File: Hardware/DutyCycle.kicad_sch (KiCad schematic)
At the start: 42 parts, among them J1 LiPo, J2 USB, Q1 AO3400A, Q2 AO3400A, Q3 AO3401A, SW1 SW_Push, U1 AT32F421KxU7, U2 DRV8837, U3 ME6211C28M5, U5 TP4055

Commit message: feat(sch): rename +2.8v -> VDD
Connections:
- net +2.8V renamed VDD
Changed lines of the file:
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@@
 			)
 		)
-		(property "Value" "+2.8V"
-			(at 193.04 143.51 0)
+		(property "Value" "VDD"
+			(at 195.58 147.3199 0)
 			(effects
 				(font
 					(size 1.27 1.27)
 				)
+				(justify right)
 			)
 		)
@@
 			)
 		)
-		(property "Value" "+2.8V"
-			(at 73.66 140.97 0)
+		(property "Value" "VDD"
+			(at 76.2 144.7799 0)
 			(effects
 				(font
 					(size 1.27 1.27)
 				)
+				(justify left)
 			)
 		)
@@
 			)
 		)
-		(property "Value" "+2.8V"
-			(at 128.27 118.11 0)
+		(property "Value" "VDD"
+			(at 130.81 121.9199 0)
 			(effects
 				(font
 					(size 1.27 1.27)
 				)
+				(justify left)
 			)
 		)
@@
 			)
 		)
-		(property "Value" "+2.8V"
-			(at 195.58 223.52 0)
+		(property "Value" "VDD"
+			(at 198.12 227.3299 0)
 			(effects
 				(font
 					(size 1.27 1.27)
 				)
+				(justify right)
 			)
 		)
@@
 		(on_board yes)
 		(dnp no)
-		(fields_autoplaced yes)
 		(property "Reference" "#PWR026"
 			(at 342.9 57.15 0)
@@
 			)
 		)
-		(property "Value" "+2.8V"
-			(at 342.9 48.26 0)
+		(property "Value" "VDD"
+			(at 344.424 49.276 0)
 			(effects
 				(font
 					(size 1.27 1.27)
 				)
+				(justify left)
 			)
 		)
@@
 			)
 		)
-		(property "Value" "+2.8V"
-			(at 128.27 203.2 0)
+		(property "Value" "VDD"
+			(at 130.81 207.0099 0)
 			(effects
 				(font
 					(size 1.27 1.27)
 				)
+				(justify left)
 			)
 		)

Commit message: feat(Hardware): upload pcb
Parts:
- removed BZ1: Buzzer, symbol Device:Buzzer
- removed C12: 10uF, Capacitor_SMD:C_0402_1005Metric, symbol Device:C
- removed C14: 100nF, Capacitor_SMD:C_0402_1005Metric, symbol Device:C
- removed R10: 0R, Resistor_SMD:R_0402_1005Metric, symbol Device:R
- removed R8: R_Variable, symbol Device:R_Variable
- removed TP5: MOT_OUT1, TestPoint:TestPoint_Pad_D1.0mm, symbol Connector:TestPoint
- removed TP6: MOT_OUT2, TestPoint:TestPoint_Pad_D1.0mm, symbol Connector:TestPoint
- removed U2: DRV8837, Package_SON:WSON-8-1EP_2x2mm_P0.5mm_EP0.9x1.6mm, symbol Driver_Motor:DRV8837
- added J4: MOT, Connector_PinHeader_2.54mm:PinHeader_1x02_P2.54mm_Vertical, symbol Connector:Conn_01x02_Pin
- added LS1: CMT-8530S-SMT, DutyCycle:CUI_CMT-8530S-SMT, symbol DutyCycle:CMT-8530S-SMT
- added R10: 3296P-1-105, DutyCycle:TRIM_3296P-1-105, symbol DutyCycle:3296P-1-105
- J2: footprint Connector_USB:USB_C_Receptacle_G-Switch_GT-USB-7051x -> Connector_USB:USB_C_Receptacle_G-Switch_GT-USB-7010ASV
- SW1: footprint Button_Switch_SMD:SW_Push_1P1T-MP_NO_Horizontal_Alps_SKRTLAE010 -> Button_Switch_THT:SW_Tactile_SPST_Angled_PTS645Vx83-2LFS
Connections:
- net VBAT: now also LS1.P
- net at Q1.3 (D): now also LS1.N
- net MOT_OUT1: now reaches U1.14 (PB0)
- net MOT_OUT1: now also R10.1
- net MOT_OUT2: now reaches U1.15 (PB1)
- net MOT_OUT2: now also J4.2 (Pin_2)
- net DRV_IN1: no longer names the net of U1.9 (PA3)
- net DRV_IN2: no longer names the net of U1.8 (PA2)
- net DRV_SLP: no longer names the net of U1.10 (PA4)
- new net: J4.1 (Pin_1), R10.2
- no-connect marks 16 -> 18

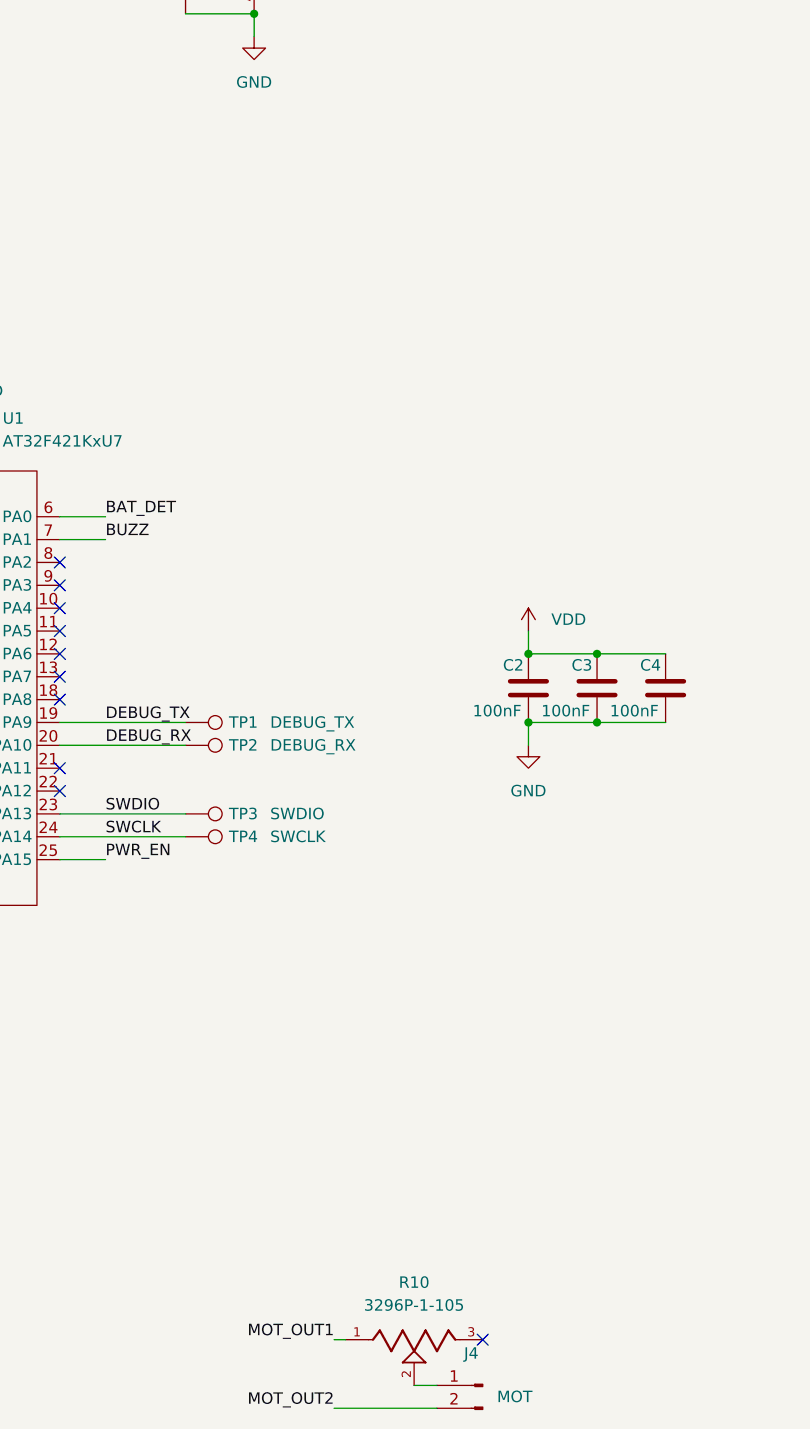
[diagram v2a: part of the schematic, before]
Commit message: feat(pcb): complete the basic layout of components
Signed-off-by: _VIFEXTech <vifextech@foxmail.com>
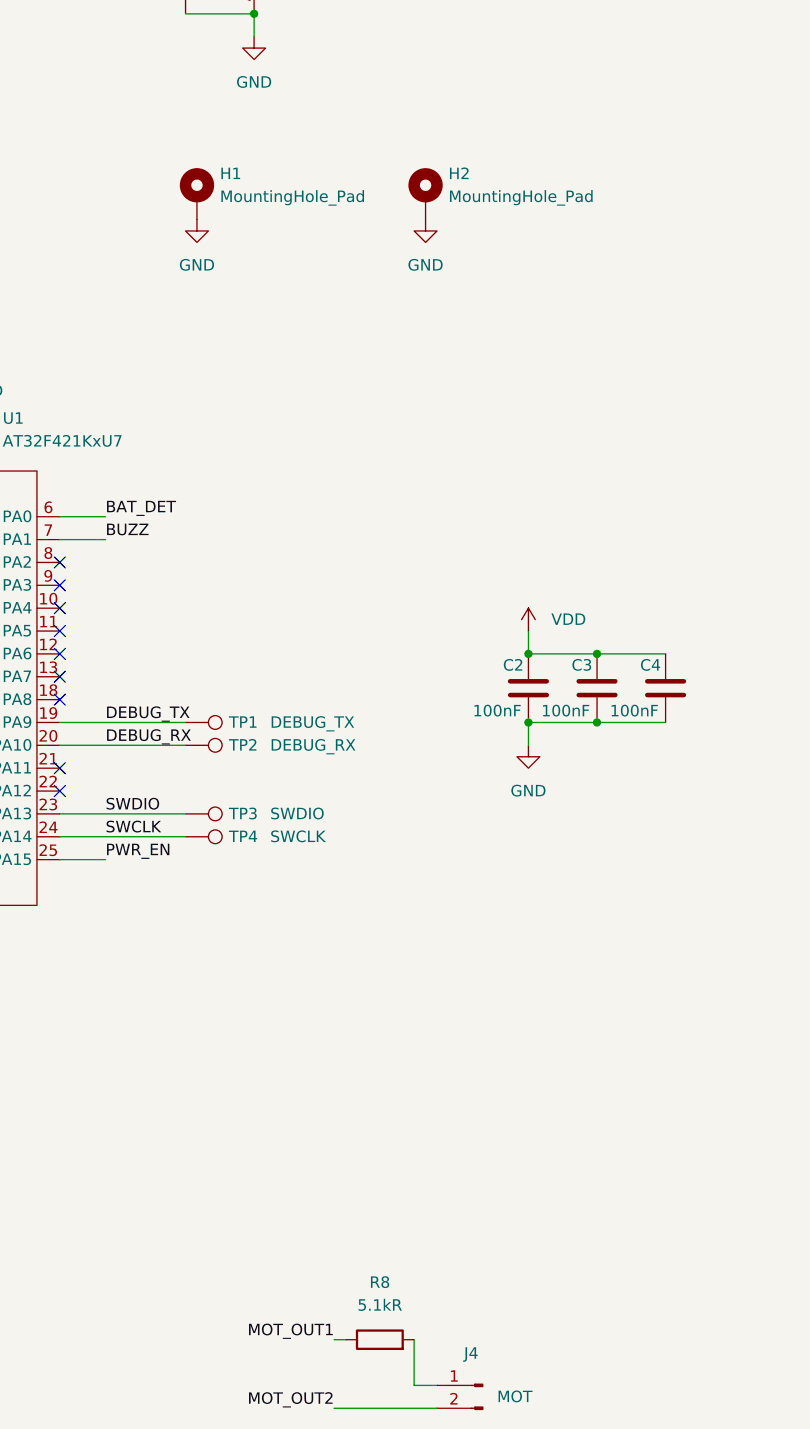
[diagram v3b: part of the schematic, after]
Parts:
- removed R10: 3296P-1-105, DutyCycle:TRIM_3296P-1-105, symbol DutyCycle:3296P-1-105
- added H1, H2: MountingHole_Pad, MountingHole:MountingHole_3.2mm_M3_Pad, symbol Mechanical:MountingHole_Pad
- added R8: 5.1kR, Resistor_SMD:R_0402_1005Metric, symbol Device:R
- J2: footprint Connector_USB:USB_C_Receptacle_G-Switch_GT-USB-7010ASV -> Connector_USB:USB_C_Receptacle_G-Switch_GT-USB-7051x
- SW1: footprint Button_Switch_THT:SW_Tactile_SPST_Angled_PTS645Vx83-2LFS -> Button_Switch_THT:SW_PUSH_6mm_H13mm
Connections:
- net GND: now also H1.1, H2.1
- net MOT_OUT1: now also R8.1
- net at J4.1 (Pin_1): now also R8.2
- no-connect marks 18 -> 17

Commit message: feat(pcb): finish PCB layout
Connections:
- net BAT_DET: now also U1.15 (PB1); no longer U1.6 (PA0)
- net BUZZ: now also U1.16 (PB2); no longer U1.7 (PA1)
- net DEBUG_RX: now also J2.A7 (D-); no longer J2.A6 (D+), J2.B6 (D+)
- net DEBUG_TX: now also J2.A8 (SBU1); no longer J2.A5 (CC1), J2.B5 (CC2)
- net KEY_DET: now also U1.14 (PB0); no longer U1.26 (PB3)
- net MOT_OUT1: now also U1.8 (PA2); no longer U1.14 (PB0)
- net MOT_OUT2: now also U1.9 (PA3); no longer U1.15 (PB1)
- net PWR_EN: now also U1.13 (PA7); no longer U1.25 (PA15)
- net SWCLK: now also J2.A5 (CC1); no longer J2.A8 (SBU1), J2.B8 (SBU2)
- net SWDIO: now also J2.A6 (D+); no longer J2.A7 (D-), J2.B7 (D-)
- no-connect marks 17 -> 21

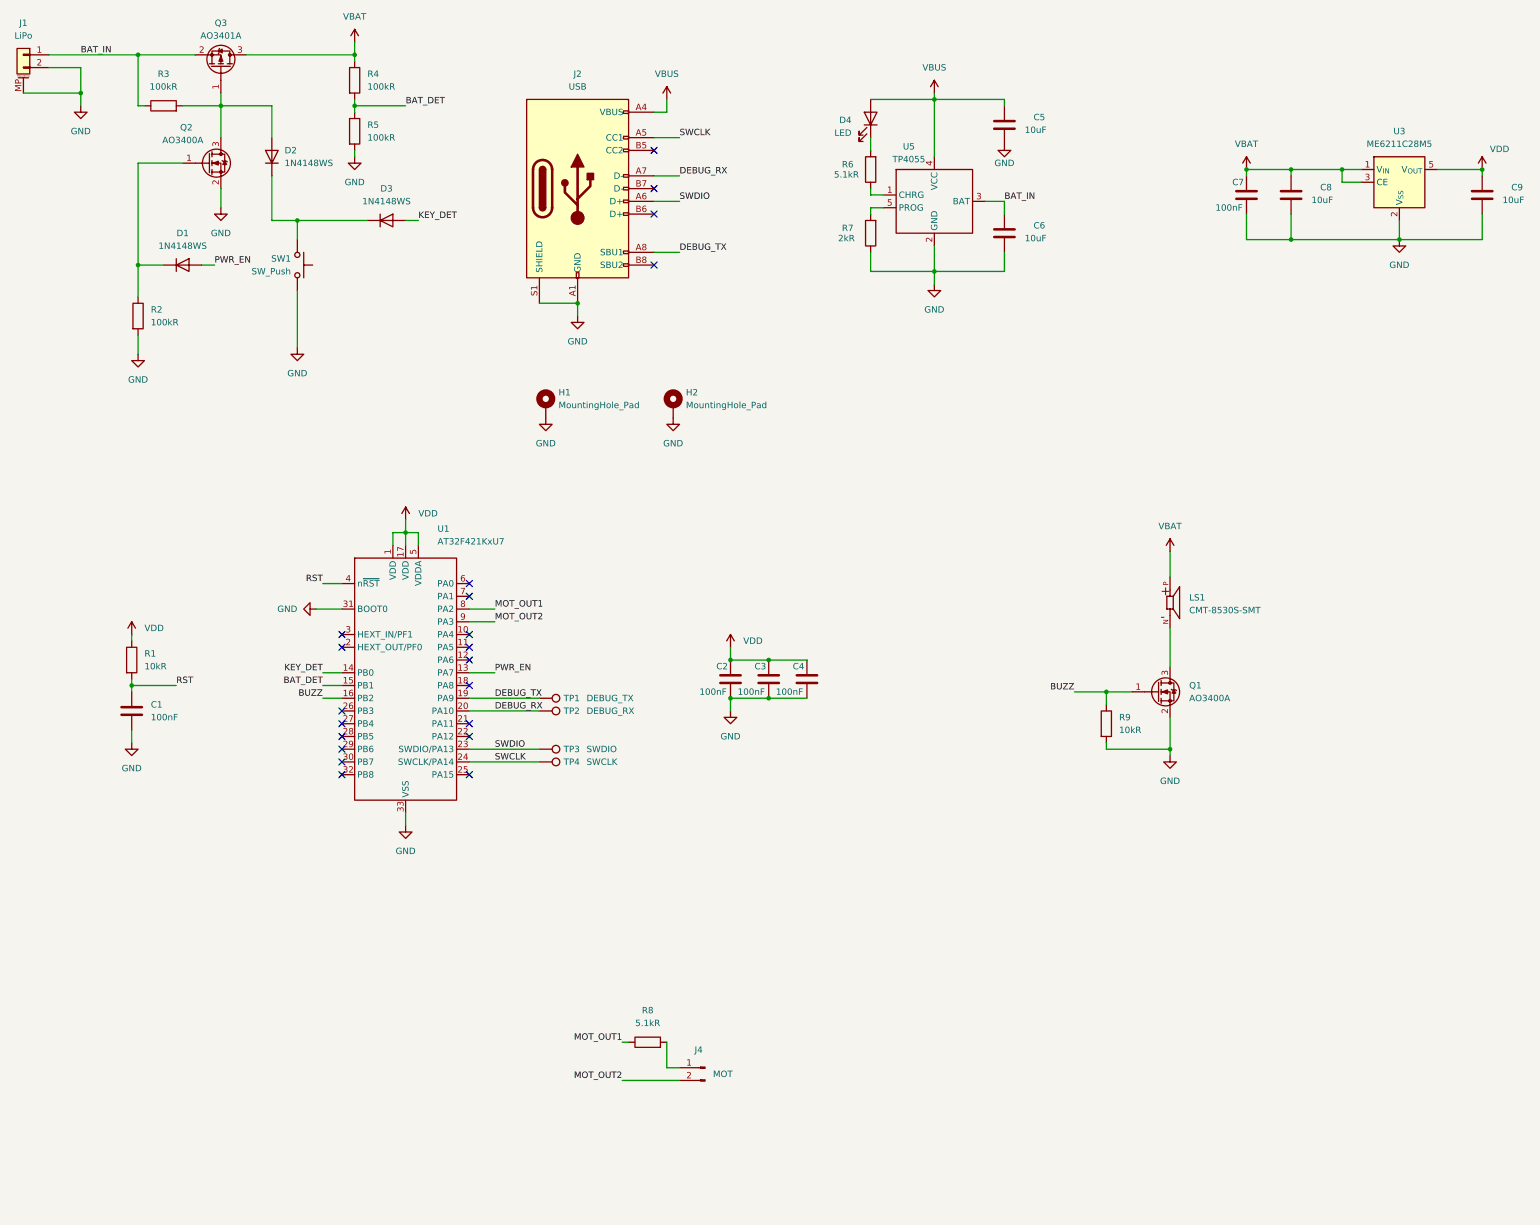
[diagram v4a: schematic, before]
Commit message: feat(Hardware): add external crystal & fix LDO packaging errors
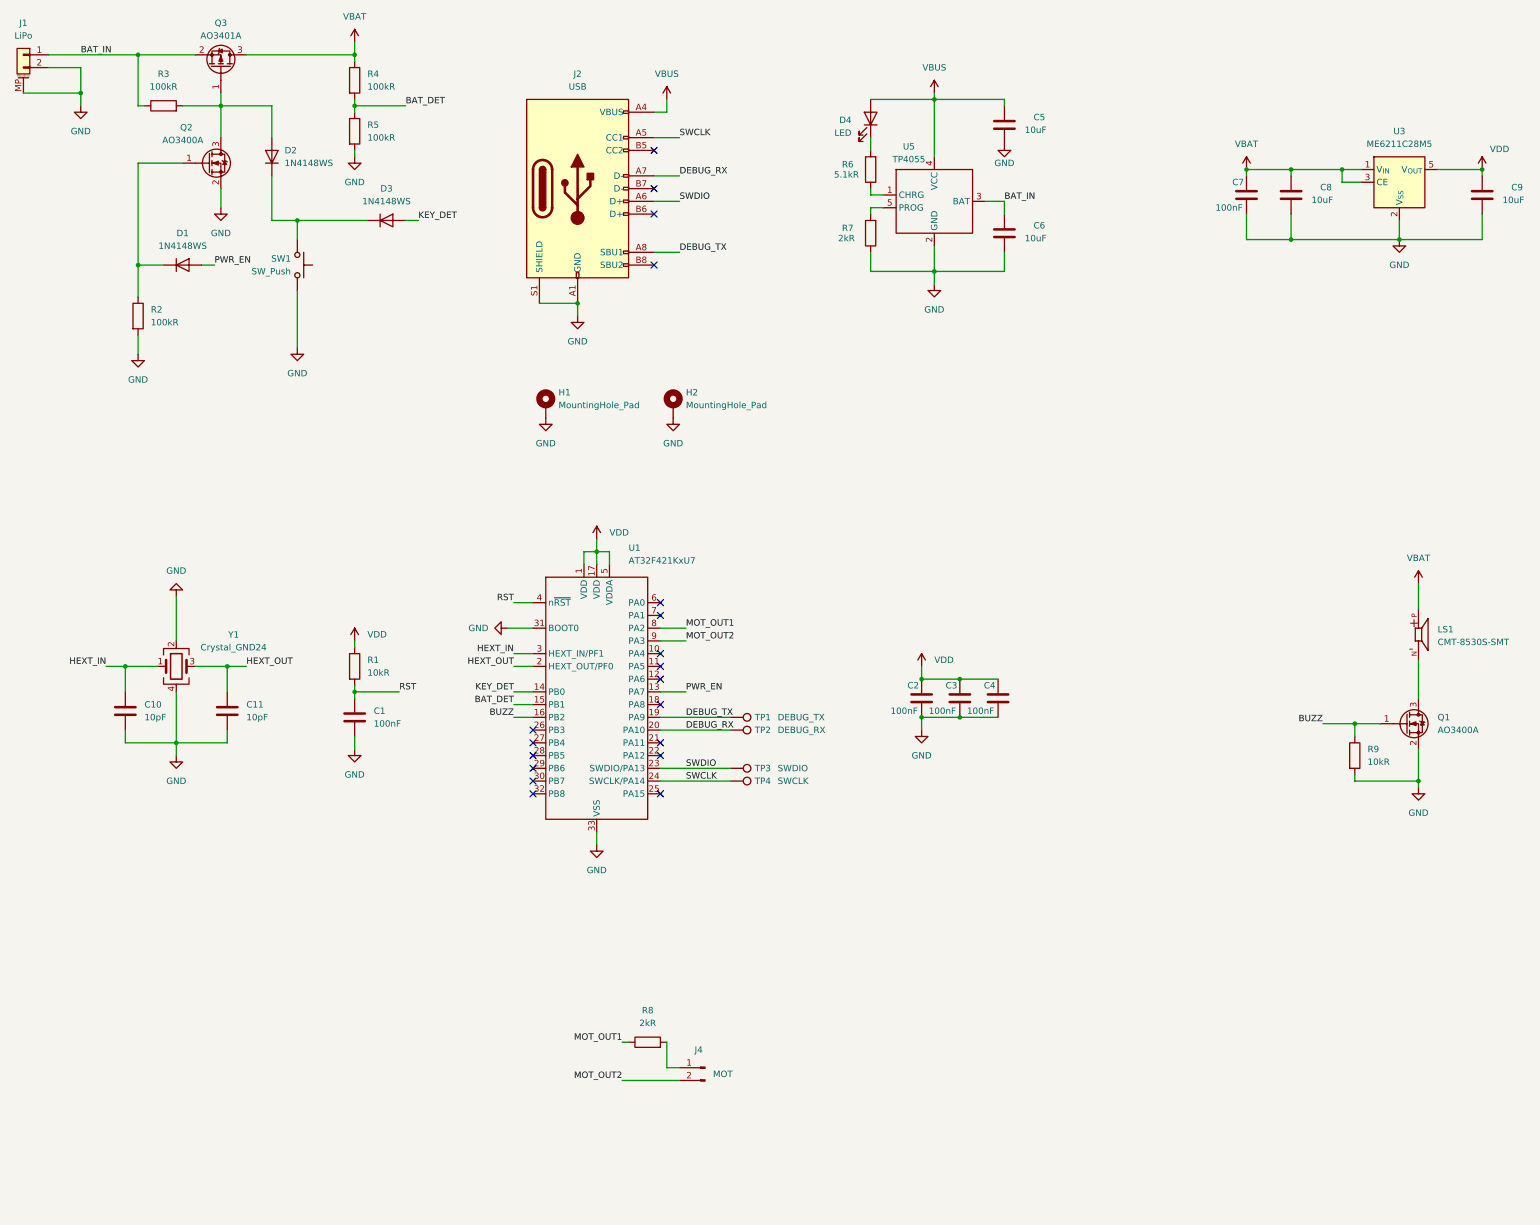
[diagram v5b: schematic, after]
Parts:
- added C10, C11: 10pF, Capacitor_SMD:C_0402_1005Metric, symbol Device:C
- added Y1: Crystal_GND24, Crystal:Crystal_SMD_3225-4Pin_3.2x2.5mm, symbol Device:Crystal_GND24
- R8: value 5.1kR -> 2kR
- U3: footprint Package_TO_SOT_SMD:SOT-23-5 -> Package_TO_SOT_SMD:SOT-353_SC-70-5
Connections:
- net GND: now also C10.2, C11.2, Y1.2, Y1.4
- net HEXT_OUT: now reaches U1.2 (HEXT_OUT/PF0)
- net HEXT_OUT: now also C11.1, Y1.3
- net HEXT_IN: now reaches U1.3 (HEXT_IN/PF1)
- net HEXT_IN: now also C10.1, Y1.1
- no-connect marks 21 -> 19
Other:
- moved on the sheet: C1, C2, C3, C4, LS1, Q1, R1, R9, TP1, TP2, TP3, TP4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

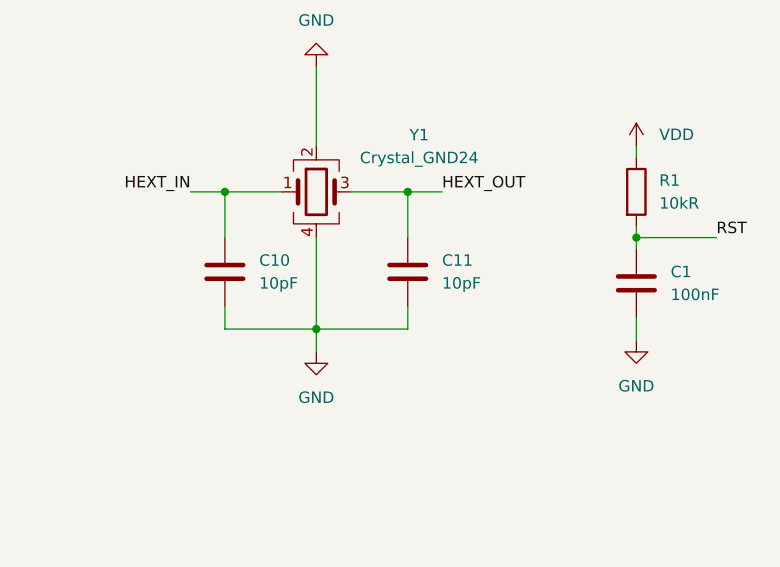
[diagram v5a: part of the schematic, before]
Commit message: fix(Hardware): change the crystal starting capacitance 10pF -> 12pF
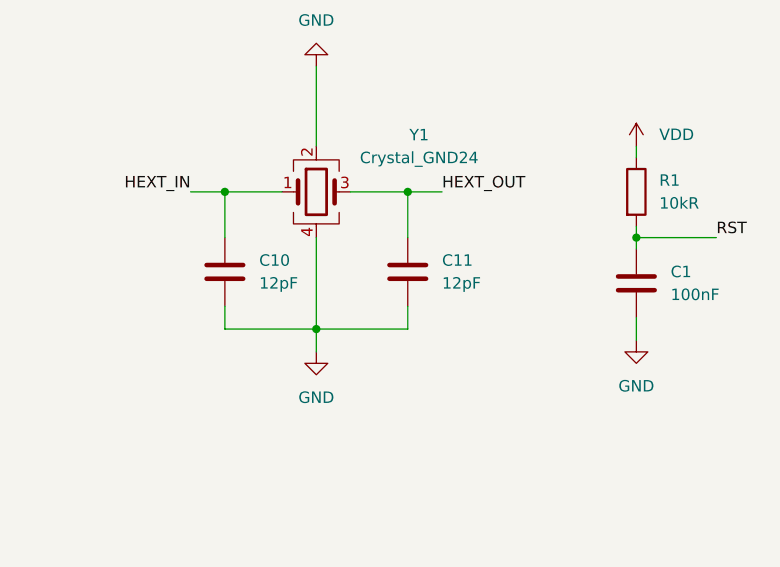
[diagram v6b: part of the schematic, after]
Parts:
- C10, C11: value 10pF -> 12pF
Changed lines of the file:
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@@
 			)
 		)
-		(property "Value" "10pF"
+		(property "Value" "12pF"
 			(at 96.52 162.5599 0)
 			(effects
@@
 			)
 		)
-		(property "Value" "10pF"
+		(property "Value" "12pF"
 			(at 76.2 162.5599 0)
 			(effects
